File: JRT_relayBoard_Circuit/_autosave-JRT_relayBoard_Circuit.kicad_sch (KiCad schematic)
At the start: 2 parts, among them J1 Conn_ESP32_Left, J2 Conn_ESP32_Right

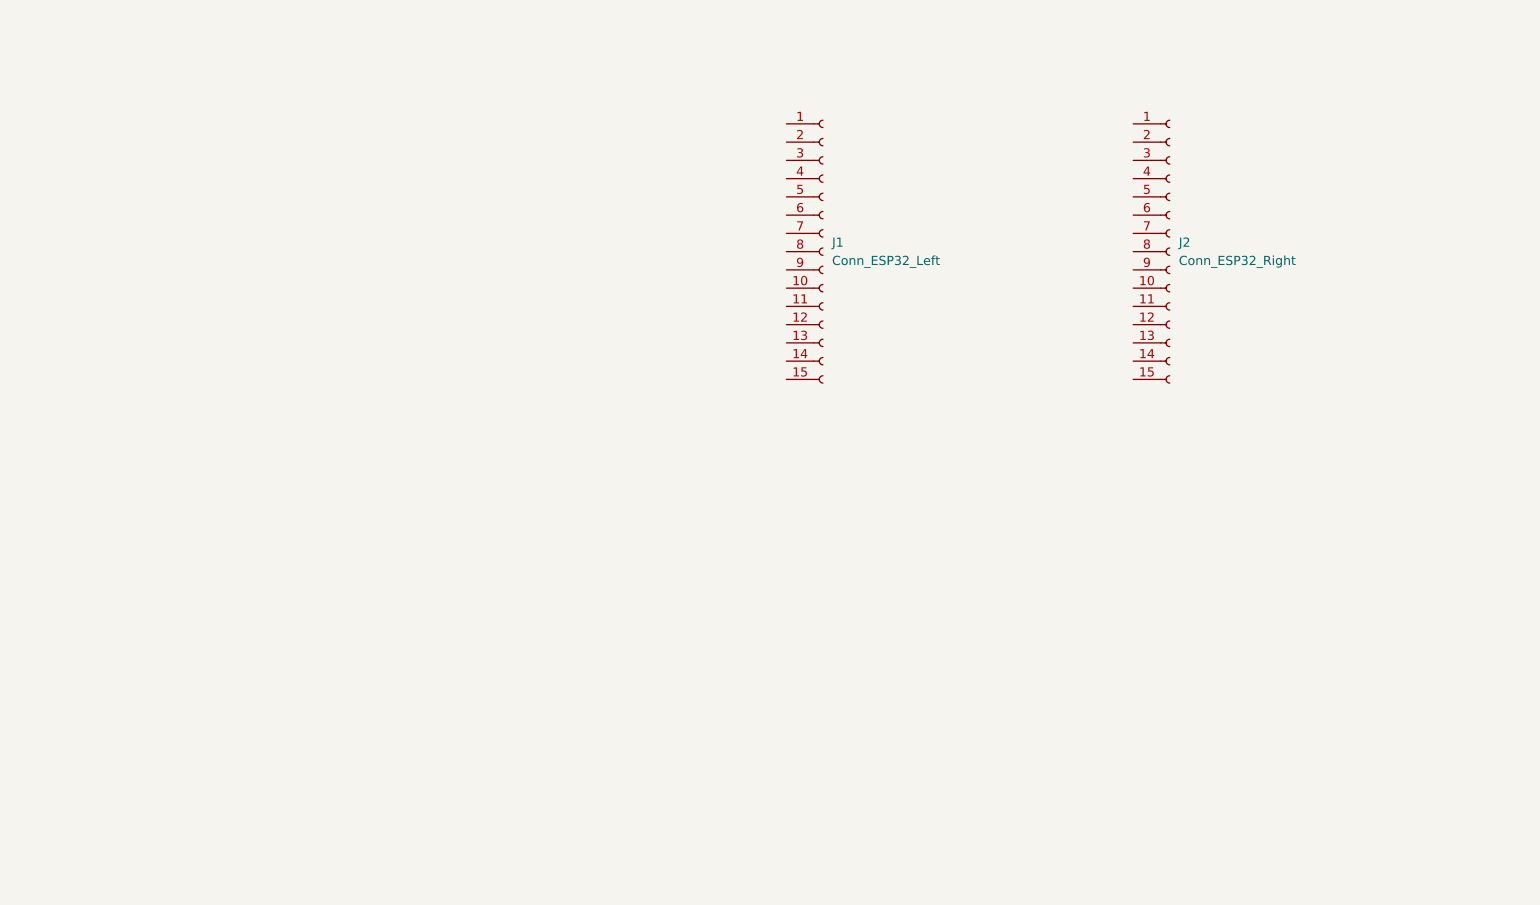
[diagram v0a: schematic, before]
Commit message: 回路図を実装
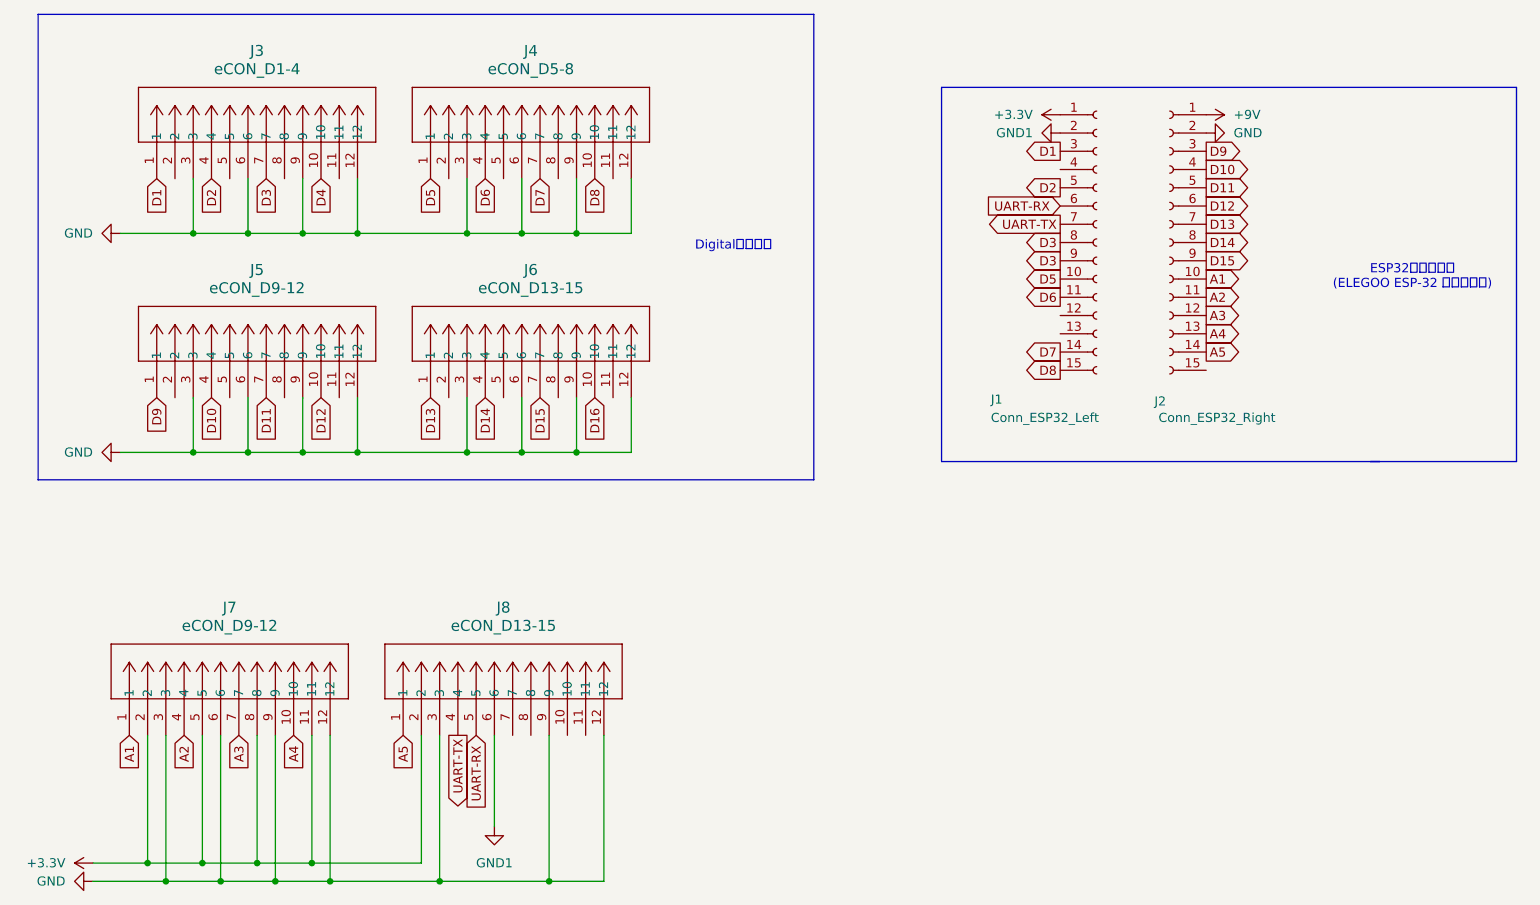
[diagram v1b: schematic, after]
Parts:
- added J3: eCON_D1-4, eCon:CONN_37212-62M3-003PL_3MM, symbol 37212_62M3_003PL:37212-62M3-003PL
- added J4: eCON_D5-8, eCon:CONN_37212-62M3-003PL_3MM, symbol 37212_62M3_003PL:37212-62M3-003PL
- added J5, J7: eCON_D9-12, eCon:CONN_37212-62M3-003PL_3MM, symbol 37212_62M3_003PL:37212-62M3-003PL
- added J6, J8: eCON_D13-15, eCon:CONN_37212-62M3-003PL_3MM, symbol 37212_62M3_003PL:37212-62M3-003PL
- J1, J2: footprint (none) -> Connector_PinSocket_1.00mm:PinSocket_1x15_P1.00mm_Vertical
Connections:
- net +9V: now reaches J2.1 (Pin_1)
- net A1: now reaches J2.10 (Pin_10)
- net A1: now also J7.1
- net A2: now reaches J2.11 (Pin_11)
- net A2: now also J7.4
- net A3: now reaches J2.12 (Pin_12)
- net A3: now also J7.7
- net A4: now reaches J2.13 (Pin_13)
- net A4: now also J7.10
- net A5: now reaches J2.14 (Pin_14)
- net A5: now also J8.1
- net GND: now reaches J2.2 (Pin_2)
- net GND: now also J3.12, J3.3, J3.6, J3.9, J4.12, J4.3, J4.6, J4.9, J5.12, J5.3, J5.6, J5.9, J6.12, J6.3, J6.6, J6.9, J7.12, J7.3, J7.6, J7.9, J8.12, J8.3, J8.9
- net D9: now reaches J2.3 (Pin_3)
- net D9: now also J5.1
- net D10: now reaches J2.4 (Pin_4)
- net D10: now also J5.4
- net D11: now reaches J2.5 (Pin_5)
- net D11: now also J5.7
- net D12: now reaches J2.6 (Pin_6)
- net D12: now also J5.10
- net D13: now reaches J2.7 (Pin_7)
- net D13: now also J6.1
- net D14: now reaches J2.8 (Pin_8)
- net D14: now also J6.4
- net D15: now reaches J2.9 (Pin_9)
- net D15: now also J6.7
- net +3.3V: now reaches J1.1 (Pin_1)
- net +3.3V: now also J7.11, J7.2, J7.5, J7.8, J8.2
- net D5: now reaches J1.10 (Pin_10)
- net D5: now also J4.1
- net D6: now reaches J1.11 (Pin_11)
- net D6: now also J4.4
- net D7: now reaches J1.14 (Pin_14)
- net D7: now also J4.7
- net D8: now reaches J1.15 (Pin_15)
- net D8: now also J4.10
- net GND1: now reaches J1.2 (Pin_2)
- net GND1: now also J8.6
- net D1: now reaches J1.3 (Pin_3)
- net D1: now also J3.1
- net D2: now reaches J1.5 (Pin_5)
- net D2: now also J3.4
- net UART-RX: now reaches J1.6 (Pin_6)
- net UART-RX: now also J8.5
- net UART-TX: now reaches J1.7 (Pin_7)
- net UART-TX: now also J8.4
- net D3: now reaches J1.8 (Pin_8)
- net D3: now also J1.9 (Pin_9), J3.7
- new net D16: J6.10
- new net D4: J3.10
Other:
- note added: "Digital入力端子"
- note added: "ESP32関係の配線 (ELEGOO ESP-32 開発ボード)"
- moved on the sheet: J1, J2
